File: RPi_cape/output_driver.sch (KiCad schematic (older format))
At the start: 21 parts, among them Q1 NTD5865NLT4G, U8 74LVC1G08, U9 EL3H7(TA)-VG

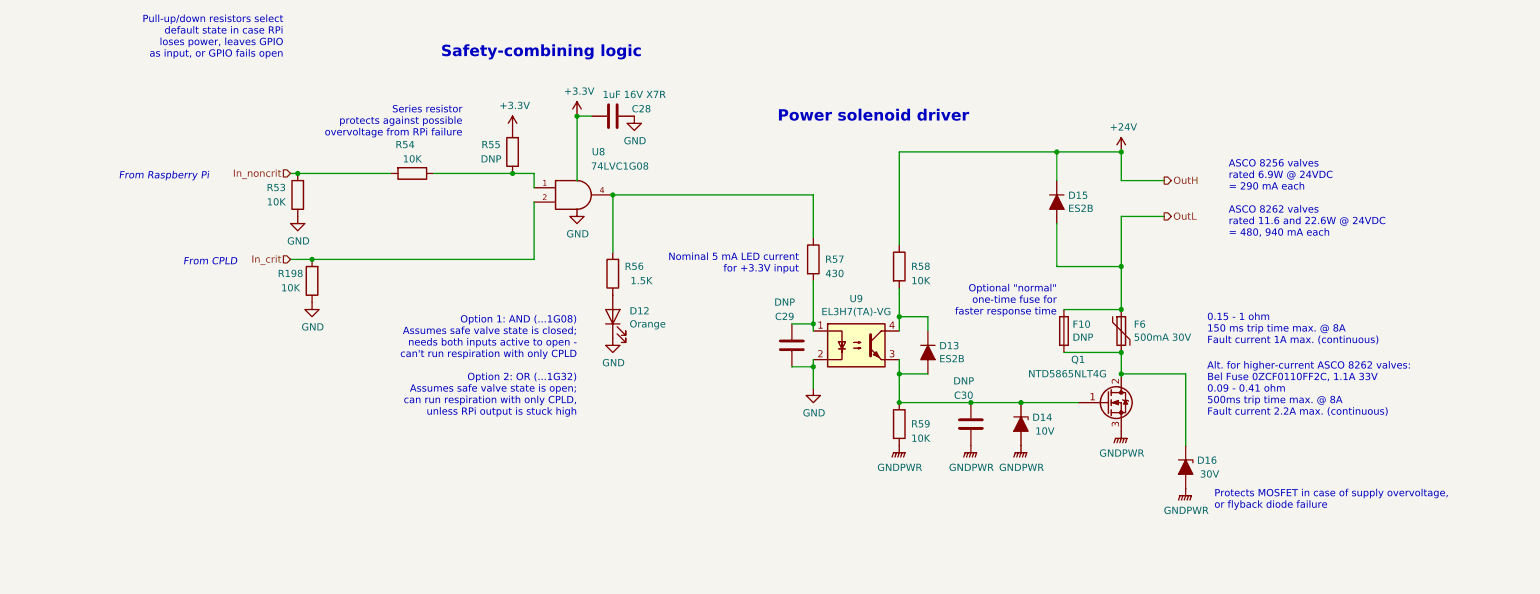
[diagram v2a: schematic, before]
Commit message: Digital pressure sensors
Added two digital pressure sensors each, on Raspberry Pi and CPLD I2C busses; preliminary layout only until mechanical details are finalized
Added gnd plane on bottom layer for heatsinking 5V regulators
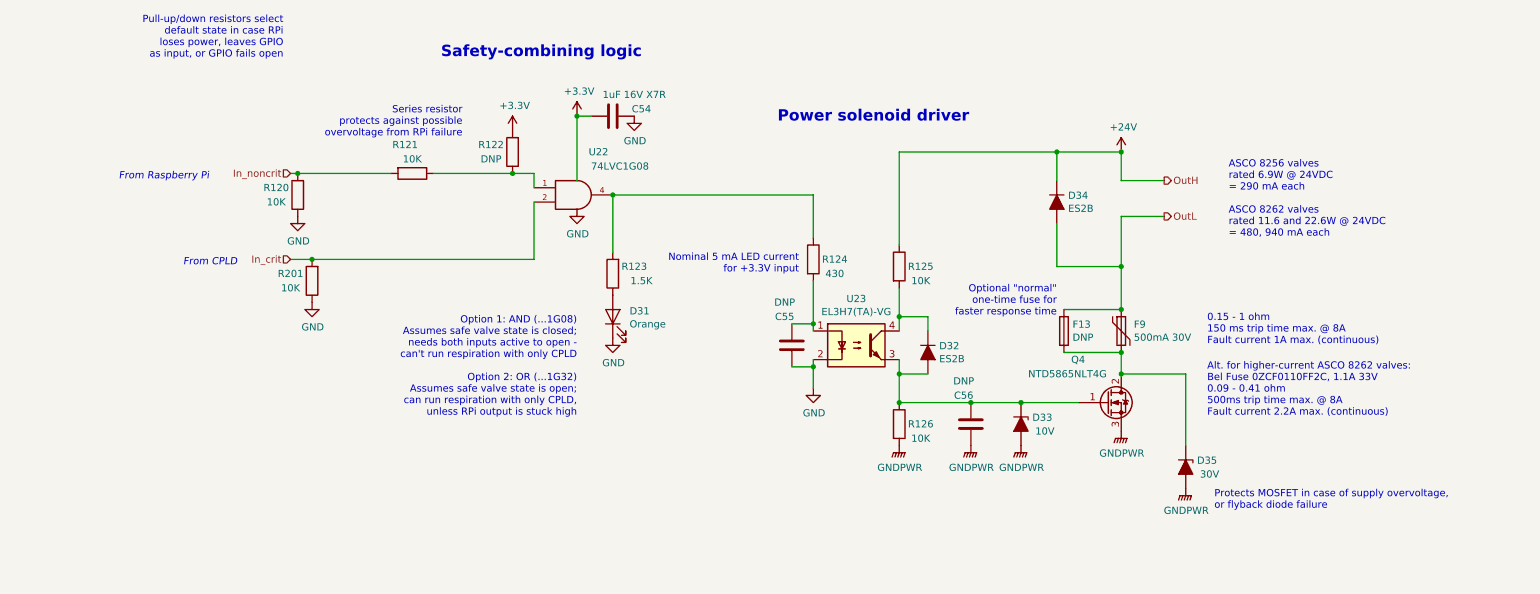
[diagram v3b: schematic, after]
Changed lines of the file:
@@
 $Descr A4 11693 8268
 encoding utf-8
-Sheet 3 12
+Sheet 3 14
 Title "Solenoid Valve Output Driver"
 Date ""
@@
 AR Path="/5E8DFCAD/5E8FC2C2" Ref="U21"  Part="1"
 AR Path="/5E8E0754/5E8FC2C2" Ref="U23"  Part="1"
-F 0 "U9" H 6450 4025 50  0000 C CNN
+F 0 "U23" H 6450 4025 50  0000 C CNN
 F 1 "EL3H7(TA)-VG" H 6450 3934 50  0000 C CNN
 F 2 "Package_SO:SOIC-4_4.55x2.6mm_P1.27mm" H 6250 3500 50  0001 L CIN
@@
 AR Path="/5E8DFCAD/5E8FF47A" Ref="R117"  Part="1"
 AR Path="/5E8E0754/5E8FF47A" Ref="R124"  Part="1"
-F 0 "R57" H 6300 3100 50  0000 C CNN
+F 0 "R124" H 6300 3100 50  0000 C CNN
 F 1 "430" H 6300 3000 50  0000 C CNN
 F 2 "Resistor_SMD:R_1206_3216Metric" V 6080 3100 50  0001 C CNN
@@
 AR Path="/5E8DFCAD/5E900D57" Ref="#PWR0183"  Part="1"
 AR Path="/5E8E0754/5E900D57" Ref="#PWR0196"  Part="1"
-F 0 "#PWR0106" H 6150 3750 50  0001 C CNN
+F 0 "#PWR0196" H 6150 3750 50  0001 C CNN
 F 1 "GND" H 6155 3827 50  0000 C CNN
 F 2 "" H 6150 4000 50  0001 C CNN
@@
 AR Path="/5E8DFCAD/5E901311" Ref="R118"  Part="1"
 AR Path="/5E8E0754/5E901311" Ref="R125"  Part="1"
-F 0 "R58" H 6900 3150 50  0000 C CNN
+F 0 "R125" H 6900 3150 50  0000 C CNN
 F 1 "10K" H 6900 3050 50  0000 C CNN
 F 2 "Resistor_SMD:R_1206_3216Metric" V 6680 3150 50  0001 C CNN
@@
 AR Path="/5E8DFCAD/5E9015BE" Ref="R119"  Part="1"
 AR Path="/5E8E0754/5E9015BE" Ref="R126"  Part="1"
-F 0 "R59" H 6900 4250 50  0000 C CNN
+F 0 "R126" H 6900 4250 50  0000 C CNN
 F 1 "10K" H 6900 4150 50  0000 C CNN
 F 2 "Resistor_SMD:R_1206_3216Metric" V 6680 4250 50  0001 C CNN
@@
 AR Path="/5E8DFCAD/5E905A02" Ref="C53"  Part="1"
 AR Path="/5E8E0754/5E905A02" Ref="C56"  Part="1"
-F 0 "C30" H 7200 4050 50  0000 C CNN
+F 0 "C56" H 7200 4050 50  0000 C CNN
 F 1 "DNP" H 7200 3950 50  0000 C CNN
 F 2 "Capacitor_SMD:C_0805_2012Metric" H 7288 4100 50  0001 C CNN
@@
 AR Path="/5E8DFCAD/5E9088A7" Ref="D28"  Part="1"
 AR Path="/5E8E0754/5E9088A7" Ref="D33"  Part="1"
-F 0 "D14" V 7554 4329 50  0000 L CNN
+F 0 "D33" V 7554 4329 50  0000 L CNN
 F 1 "10V" V 7650 4350 50  0000 L CNN
 F 2 "Diode_SMD:D_SOD-123" H 7600 4250 50  0001 C CNN
@@
 AR Path="/5E8DFCAD/5E908F8A" Ref="Q3"  Part="1"
 AR Path="/5E8E0754/5E908F8A" Ref="Q4"  Part="1"
-F 0 "Q1" H 7950 4400 50  0000 L CNN
+F 0 "Q4" H 7950 4400 50  0000 L CNN
 F 1 "NTD5865NLT4G" H 7650 4300 50  0000 L CNN
 F 2 "Package_TO_SOT_SMD:TO-252-2" H 8400 4200 50  0001 C CNN
@@
 AR Path="/5E8DFCAD/5E909869" Ref="F8"  Part="1"
 AR Path="/5E8E0754/5E909869" Ref="F9"  Part="1"
-F 0 "F6" H 8388 3646 50  0000 L CNN
+F 0 "F9" H 8388 3646 50  0000 L CNN
 F 1 "500mA 30V" H 8388 3555 50  0000 L CNN
 F 2 "Fuse:Fuse_2920_7451Metric" H 8350 3400 50  0001 L CNN
@@
 AR Path="/5E8DFCAD/5E90C94B" Ref="D30"  Part="1"
 AR Path="/5E8E0754/5E90C94B" Ref="D35"  Part="1"
-F 0 "D16" V 8704 4629 50  0000 L CNN
+F 0 "D35" V 8704 4629 50  0000 L CNN
 F 1 "30V" V 8800 4650 50  0000 L CNN
 F 2 "Diode_SMD:D_SMA" H 8750 4550 50  0001 C CNN
@@
 AR Path="/5E8DFCAD/5E90D582" Ref="D29"  Part="1"
 AR Path="/5E8E0754/5E90D582" Ref="D34"  Part="1"
-F 0 "D15" V 7804 2779 50  0000 L CNN
+F 0 "D34" V 7804 2779 50  0000 L CNN
 F 1 "ES2B" V 7895 2779 50  0000 L CNN
 F 2 "Diode_SMD:D_SMA" H 7850 2700 50  0001 C CNN
@@
 AR Path="/5E8DFCAD/5E913275" Ref="D27"  Part="1"
 AR Path="/5E8E0754/5E913275" Ref="D32"  Part="1"
-F 0 "D13" V 6904 3829 50  0000 L CNN
+F 0 "D32" V 6904 3829 50  0000 L CNN
 F 1 "ES2B" V 6995 3829 50  0000 L CNN
 F 2 "Diode_SMD:D_SMA" H 6950 3750 50  0001 C CNN
@@
 AR Path="/5E8DFCAD/5E880DD0" Ref="#PWR0189"  Part="1"
 AR Path="/5E8E0754/5E880DD0" Ref="#PWR0202"  Part="1"
-F 0 "#PWR0112" H 8750 4500 50  0001 C CNN
+F 0 "#PWR0202" H 8750 4500 50  0001 C CNN
 F 1 "GNDPWR" H 8754 4546 50  0000 C CNN
 F 2 "" H 8750 4650 50  0001 C CNN
@@
 AR Path="/5E8DFCAD/5E8842DE" Ref="#PWR0187"  Part="1"
 AR Path="/5E8E0754/5E8842DE" Ref="#PWR0200"  Part="1"
-F 0 "#PWR0110" H 8300 2200 50  0001 C CNN
+F 0 "#PWR0200" H 8300 2200 50  0001 C CNN
 F 1 "+24V" H 8315 2523 50  0000 C CNN
 F 2 "" H 8300 2350 50  0001 C CNN
@@
 AR Path="/5E8DFCAD/5E88C1E4" Ref="C52"  Part="1"
 AR Path="/5E8E0754/5E88C1E4" Ref="C55"  Part="1"
-F 0 "C29" H 5950 3500 50  0000 C CNN
+F 0 "C55" H 5950 3500 50  0000 C CNN
 F 1 "DNP" H 5950 3400 50  0000 C CNN
 F 2 "Capacitor_SMD:C_0805_2012Metric" H 6038 3550 50  0001 C CNN
@@
 AR Path="/5E8DFCAD/5EA15643" Ref="U20"  Part="1"
 AR Path="/5E8DEDC0/5EA15643" Ref="U18"  Part="1"
-F 0 "U8" H 4650 2950 50  0000 C CNN
+F 0 "U22" H 4650 2950 50  0000 C CNN
 F 1 "74LVC1G08" H 4800 2850 50  0000 C CNN
 F 2 "Package_TO_SOT_SMD:SOT-23-5" H 4500 2650 50  0001 C CNN
@@
 AR Path="/5E8DFCAD/5EA17709" Ref="#PWR0180"  Part="1"
 AR Path="/5E8E0754/5EA17709" Ref="#PWR0193"  Part="1"
-F 0 "#PWR0103" H 4500 2500 50  0001 C CNN
+F 0 "#PWR0193" H 4500 2500 50  0001 C CNN
 F 1 "GND" H 4505 2577 50  0000 C CNN
 F 2 "" H 4500 2750 50  0001 C CNN
@@
 AR Path="/5E8DFCAD/5EA197B0" Ref="#PWR0179"  Part="1"
 AR Path="/5E8DEDC0/5EA197B0" Ref="#PWR0166"  Part="1"
-F 0 "#PWR0102" H 4500 1950 50  0001 C CNN
+F 0 "#PWR0192" H 4500 1950 50  0001 C CNN
 F 1 "+3.3V" H 4515 2273 50  0000 C CNN
 F 2 "" H 4500 2100 50  0001 C CNN
@@
 AR Path="/5E8DFCAD/5EA25A46" Ref="#PWR0182"  Part="1"
 AR Path="/5E8DEDC0/5EA25A46" Ref="#PWR0169"  Part="1"
-F 0 "#PWR0105" H 4900 1850 50  0001 C CNN
+F 0 "#PWR0195" H 4900 1850 50  0001 C CNN
 F 1 "GND" H 4905 1927 50  0000 C CNN
 F 2 "" H 4900 2100 50  0001 C CNN
@@
 AR Path="/5E8DFCAD/5EA25A4C" Ref="C51"  Part="1"
 AR Path="/5E8DEDC0/5EA25A4C" Ref="C48"  Part="1"
-F 0 "C28" V 4700 2300 50  0000 C CNN
+F 0 "C54" V 4700 2300 50  0000 C CNN
 F 1 "1uF 16V X7R" V 4600 2250 50  0000 C CNN
 F 2 "Capacitor_SMD:C_0805_2012Metric" H 4788 1950 50  0001 C CNN
@@
 AR Path="/5E8DFCAD/5EAB3FCE" Ref="R113"  Part="1"
 AR Path="/5E8E0754/5EAB3FCE" Ref="R120"  Part="1"
-F 0 "R53" H 2700 2600 50  0000 C CNN
+F 0 "R120" H 2700 2600 50  0000 C CNN
 F 1 "10K" H 2700 2700 50  0000 C CNN
 F 2 "Resistor_SMD:R_1206_3216Metric" V 2480 2650 50  0001 C CNN
@@
 AR Path="/5E8DFCAD/5EAB68F6" Ref="#PWR0177"  Part="1"
 AR Path="/5E8E0754/5EAB68F6" Ref="#PWR0190"  Part="1"
-F 0 "#PWR0100" H 2550 2550 50  0001 C CNN
+F 0 "#PWR0190" H 2550 2550 50  0001 C CNN
 F 1 "GND" H 2555 2627 50  0000 C CNN
 F 2 "" H 2550 2800 50  0001 C CNN
@@
 AR Path="/5E8DFCAD/5EB47B74" Ref="R115"  Part="1"
 AR Path="/5E8E0754/5EB47B74" Ref="R122"  Part="1"
-F 0 "R55" H 4200 2300 50  0000 C CNN
+F 0 "R122" H 4200 2300 50  0000 C CNN
 F 1 "DNP" H 4200 2400 50  0000 C CNN
 F 2 "Resistor_SMD:R_1206_3216Metric" V 3980 2350 50  0001 C CNN
@@
 AR Path="/5E8DFCAD/5EB49CAF" Ref="#PWR0178"  Part="1"
 AR Path="/5E8DEDC0/5EB49CAF" Ref="#PWR0165"  Part="1"
-F 0 "#PWR0101" H 4050 2050 50  0001 C CNN
+F 0 "#PWR0191" H 4050 2050 50  0001 C CNN
 F 1 "+3.3V" H 4065 2373 50  0000 C CNN
 F 2 "" H 4050 2200 50  0001 C CNN
@@
 AR Path="/5E8DFCAD/5EA292AA" Ref="R114"  Part="1"
 AR Path="/5E8E0754/5EA292AA" Ref="R121"  Part="1"
-F 0 "R54" V 3150 2450 50  0000 C CNN
+F 0 "R121" V 3150 2450 50  0000 C CNN
 F 1 "10K" V 3250 2500 50  0000 C CNN
 F 2 "Resistor_SMD:R_1206_3216Metric" V 3280 2500 50  0001 C CNN
@@
 AR Path="/5E8DFCAD/5F8B2D08" Ref="D26"  Part="1"
 AR Path="/5E8E0754/5F8B2D08" Ref="D31"  Part="1"
-F 0 "D12" V 4789 3383 50  0000 R CNN
+F 0 "D31" V 4789 3383 50  0000 R CNN
 F 1 "Orange" V 4698 3383 50  0000 R CNN
 F 2 "LED_SMD:LED_0805_2012Metric" H 4750 3500 50  0001 C CNN
@@
 AR Path="/5E8DEDC0/5F8B2D0E" Ref="#PWR0168"  Part="1"
 AR Path="/5E8C8865/5F8B2D0E" Ref="#PWR?"  Part="1"
-F 0 "#PWR0104" H 4750 3400 50  0001 C CNN
+F 0 "#PWR0194" H 4750 3400 50  0001 C CNN
 F 1 "GND" H 4755 3477 50  0000 C CNN
 F 2 "" H 4750 3650 50  0001 C CNN
@@
 AR Path="/5E8DFCAD/5F8B2D14" Ref="R116"  Part="1"
 AR Path="/5E8E0754/5F8B2D14" Ref="R123"  Part="1"
-F 0 "R56" H 4600 3150 50  0000 C CNN
+F 0 "R123" H 4600 3150 50  0000 C CNN
 F 1 "1.5K" H 4550 3250 50  0000 C CNN
 F 2 "Resistor_SMD:R_1206_3216Metric" V 4680 3200 50  0001 C CNN
@@
 AR Path="/5E8DFCAD/5FA3BD23" Ref="F12"  Part="1"
 AR Path="/5E8E0754/5FA3BD23" Ref="F13"  Part="1"
-F 0 "F10" H 7960 3646 50  0000 L CNN
+F 0 "F13" H 7960 3646 50  0000 L CNN
 F 1 "DNP" H 7960 3555 50  0000 L CNN
 F 2 "Fuse:Fuse_1206_3216Metric" V 7830 3600 50  0001 C CNN
@@
 AR Path="/5E8DFCAD/5E882AC5" Ref="#PWR0184"  Part="1"
 AR Path="/5E8E0754/5E882AC5" Ref="#PWR0197"  Part="1"
-F 0 "#PWR0107" H 6750 4200 50  0001 C CNN
+F 0 "#PWR0197" H 6750 4200 50  0001 C CNN
 F 1 "GNDPWR" H 6754 4246 50  0000 C CNN
 F 2 "" H 6750 4350 50  0001 C CNN
@@
 AR Path="/5E8DFCAD/5E88277D" Ref="#PWR0185"  Part="1"
 AR Path="/5E8E0754/5E88277D" Ref="#PWR0198"  Part="1"
-F 0 "#PWR0108" H 7250 4200 50  0001 C CNN
+F 0 "#PWR0198" H 7250 4200 50  0001 C CNN
 F 1 "GNDPWR" H 7254 4246 50  0000 C CNN
 F 2 "" H 7250 4350 50  0001 C CNN
@@
 AR Path="/5E8DFCAD/5E882430" Ref="#PWR0186"  Part="1"
 AR Path="/5E8E0754/5E882430" Ref="#PWR0199"  Part="1"
-F 0 "#PWR0109" H 7600 4200 50  0001 C CNN
+F 0 "#PWR0199" H 7600 4200 50  0001 C CNN
 F 1 "GNDPWR" H 7604 4246 50  0000 C CNN
 F 2 "" H 7600 4350 50  0001 C CNN
@@
 AR Path="/5E8DFCAD/5E881F2F" Ref="#PWR0188"  Part="1"
 AR Path="/5E8E0754/5E881F2F" Ref="#PWR0201"  Part="1"
-F 0 "#PWR0111" H 8300 4100 50  0001 C CNN
+F 0 "#PWR0201" H 8300 4100 50  0001 C CNN
 F 1 "GNDPWR" H 8304 4146 50  0000 C CNN
 F 2 "" H 8300 4250 50  0001 C CNN
@@
 AR Path="/5E8DFCAD/5F439429" Ref="R200"  Part="1"
 AR Path="/5E8E0754/5F439429" Ref="R201"  Part="1"
-F 0 "R198" H 2800 3200 50  0000 C CNN
+F 0 "R201" H 2800 3200 50  0000 C CNN
 F 1 "10K" H 2800 3300 50  0000 C CNN
 F 2 "Resistor_SMD:R_1206_3216Metric" V 2580 3250 50  0001 C CNN
@@
 AR Path="/5E8DFCAD/5F439819" Ref="#PWR0279"  Part="1"
 AR Path="/5E8E0754/5F439819" Ref="#PWR0280"  Part="1"
-F 0 "#PWR0275" H 2650 3150 50  0001 C CNN
+F 0 "#PWR0280" H 2650 3150 50  0001 C CNN
 F 1 "GND" H 2655 3227 50  0000 C CNN
 F 2 "" H 2650 3400 50  0001 C CNN

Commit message: Better valve monitoring, finalized layout and manufacturing files
Created assembly and fabrication drawings, assigned all BOM parts, generally made design ready for ordering
Added strain-relief slots and barb mounting dimensions for digital pressure sensors
Changed valve drivers from discrete power MOSFETs to "smart" industrial/automotive driver ICs for the current monitoring, including valve-movement monitor for #4
Connected RPi_Valve* signals to larger CPLD footprint, changed Raspberry Pi pin assignment as a result to ease PCB routing
Updated footprints, page layout to create readable assembly drawing
Added current-measurement testpoints for CPLD power from BATT+
Changed power diodes in power-down-alarm circuit to small-signal parts for more compact layout
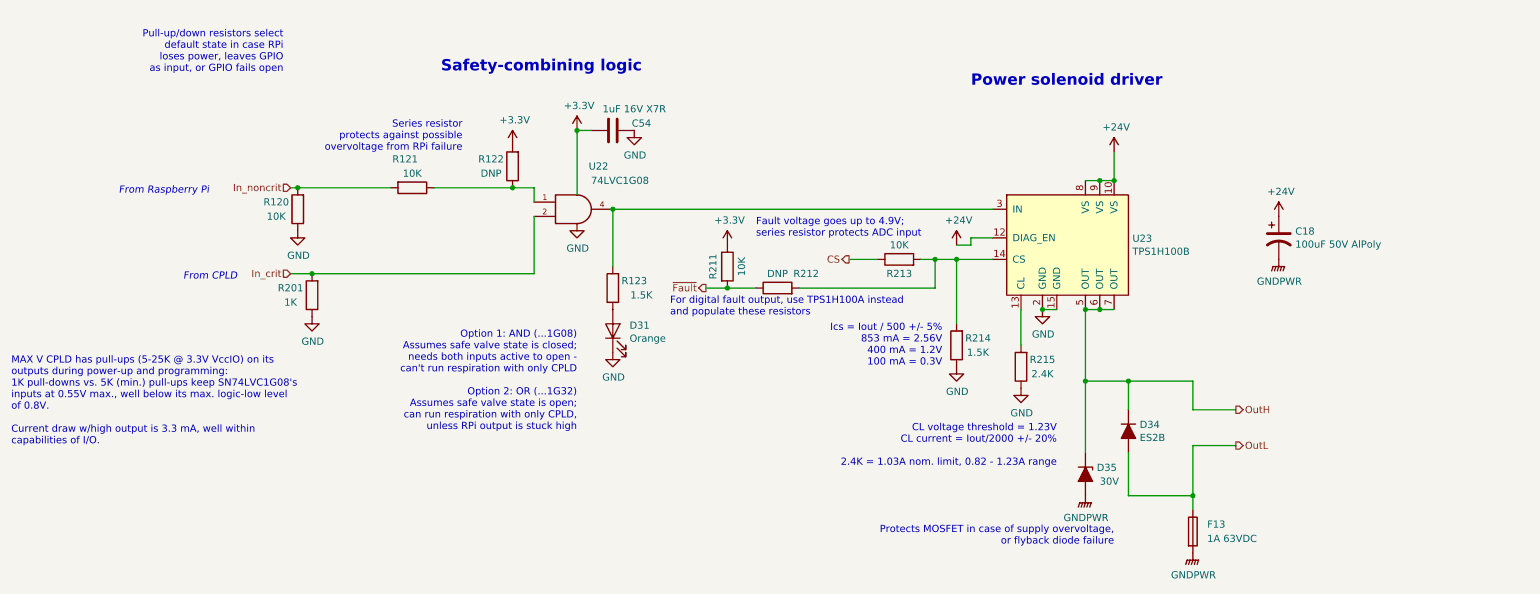
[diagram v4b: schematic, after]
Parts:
- removed C29, C30: DNP, Capacitor_SMD:C_0805_2012Metric, symbol Device:C
- removed D13: ES2B, Diode_SMD:D_SMA, symbol Device:D_ALT
- removed D14: 10V, Diode_SMD:D_SOD-123, symbol Device:D_Zener_ALT
- removed F6: 500mA 30V, Fuse:Fuse_2920_7451Metric, symbol Device:Polyfuse
- removed Q1: NTD5865NLT4G, Package_TO_SOT_SMD:TO-252-2, symbol Device:Q_NMOS_GDS
- removed U9: EL3H7(TA)-VG, Package_SO:SOIC-4_4.55x2.6mm_P1.27mm, symbol Isolator:TLP291
- added C16: 100uF 50V AlPoly, Capacitor_SMD:CP_Elec_10x10.5, symbol Device:CP1
- added R110: 1.5K, Resistor_SMD:R_1206_3216Metric, symbol Device:R
- added R111: 2.4K, Resistor_SMD:R_1206_3216Metric, symbol Device:R
- added U9: TPS1H100B, Ventilator:TSSOP-14-1EP_4.4x5mm_P0.65mm, symbol Ventilator:TPS1H100B
- D12: footprint LED_SMD:LED_0805_2012Metric -> Ventilator:LED_0805_2012Metric
- D15, D16: footprint Diode_SMD:D_SMA -> Ventilator:D_SMA
- F10: value DNP -> 1A 63VDC; Manufacturer (none) -> Bourns; Part Number (none) -> SF-1206FP100-2
- R198: value 10K -> 1K; Manufacturer (none) -> KOA Speer; Part Number (none) -> RK73H2BTTD1001F
- R53, R54, R59: Manufacturer (none) -> KOA Speer; Part Number (none) -> RK73H2BTTD1002F
- R56: Manufacturer (none) -> KOA Speer; Part Number (none) -> RK73H2BTTD1501F
- R57: value 430 -> 10K; Manufacturer (none) -> KOA Speer; Part Number (none) -> RK73H2BTTD1002F
- R58: value 10K -> DNP
- U8: footprint Package_TO_SOT_SMD:SOT-23-5 -> Ventilator:SOT-23-5; Manufacturer (none) -> Texas Instruments; Part Number (none) -> SN74LVC1G08DBVR
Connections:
- net +24V: now also C16.1, U9.10 (VS), U9.12 (DIAG_EN), U9.8 (VS), U9.9 (VS); no longer D15.1 (K), R58.1
- net +3V3: now also R57.1
- net GND: now also R110.1, R111.1, U9.15 (GND), U9.2 (GND)
- net GNDPWR: now also F10.2, C16.2; no longer R59.2
- net ~Fault: now reaches R57.2
- net ~Fault: now also R58.1
- net CS: now reaches R59.1
- net at R58.2: now also R59.2, R110.2, U9.14 (CS)
- net at R56.2, U8.4: now also U9.3 (IN); no longer R57.1
- net OutH: now reaches D16.1 (K)
- net OutH: now also D15.1 (K), U9.5 (OUT), U9.6 (OUT), U9.7 (OUT); no longer F10.2
- new net: R111.2, U9.13 (CL)
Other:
- note added: "CL voltage threshold = 1.23V\nCL current = Iout/2000 +/- 20%\n\n2.4K = 1.03A nom. limit, 0.82 - 1.23A range"
- note added: "Fault voltage goes up to 4.9V;\nseries resistor protects ADC input"
- note added: "For digital fault output, use TPS1H100A instead\nand populate these resistors"
- note added: "Ics = Iout / 500 +/- 5%\n853 mA = 2.56V\n400 mA = 1.2V\n100 mA = 0.3V"
- note added: "MAX V CPLD has pull-ups (5-25K @ 3.3V VccIO) on its\noutputs during power-up and programming:\n1K pull-downs vs. 5K (min.) pull-ups keep SN74LVC1G08's\ninputs at 0.55V max., well below its max. logic-low level\nof 0.8V.\n\nCurrent draw w/high output is 3.3 mA, well within\ncapabilities of I/O."
- note removed: "0.15 - 1 ohm\n150 ms trip time max. @ 8A\nFault current 1A max. (continuous)"
- note removed: "ASCO 8256 valves\nrated 6.9W @ 24VDC\n= 290 mA each\n\nASCO 8262 valves\nrated 11.6 and 22.6W @ 24VDC\n= 480, 940 mA each"
- note removed: "Alt. for higher-current ASCO 8262 valves:\nBel Fuse 0ZCF0110FF2C, 1.1A 33V\n0.09 - 0.41 ohm\n500ms trip time max. @ 8A\nFault current 2.2A max. (continuous)"
- note removed: "Nominal 5 mA LED current\nfor +3.3V input"
- note removed: "Optional "normal"\none-time fuse for\nfaster response time"
- moved on the sheet: C54, D31, D34, D35, F13, R120, R121, R122, R123, R201, U22
